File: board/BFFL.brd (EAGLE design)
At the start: 51 x 25.4 mm, 25 parts, among them IC1 LM317MSTT3, Q1 FDS5680, U1 ATTINY84-20SSU

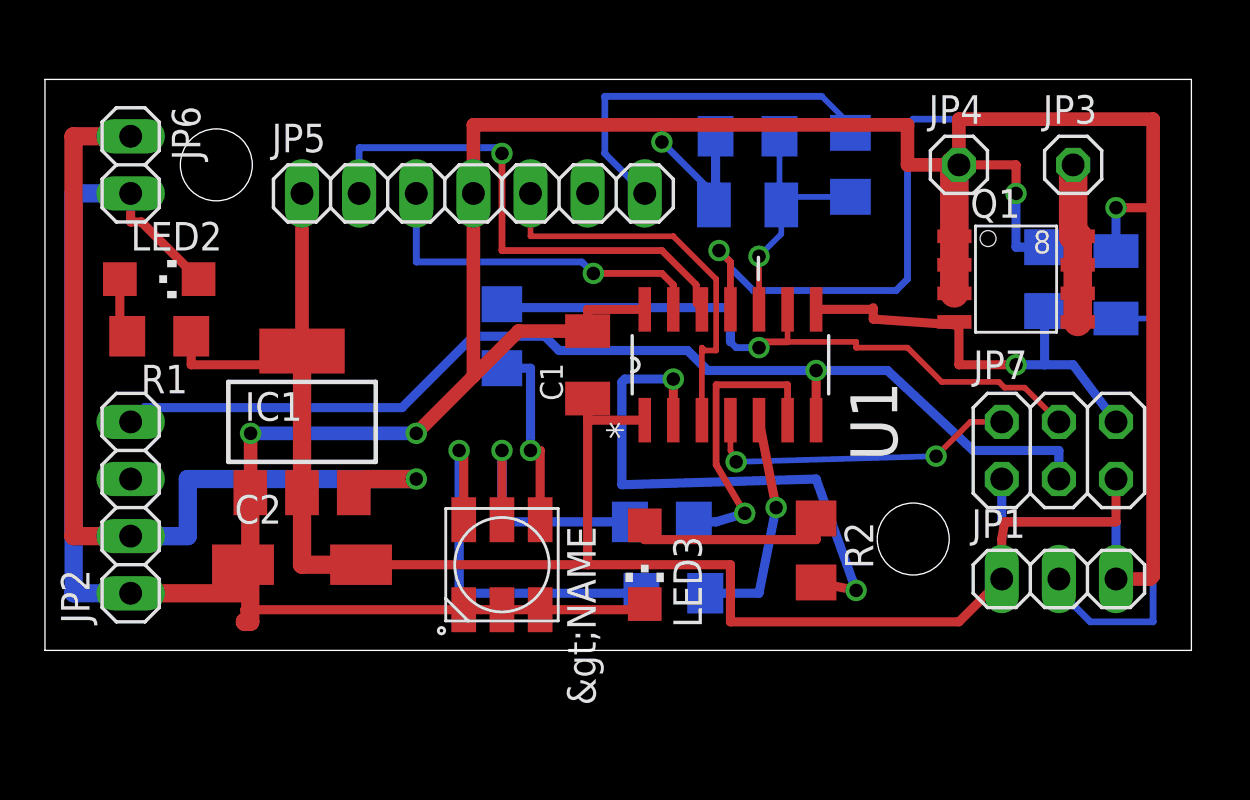
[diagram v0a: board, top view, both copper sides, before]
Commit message: Rev B of PCB, preliminary
Corrects multiple faults in Rev A and improves mounting options.
Silkscreen still needs to be done.
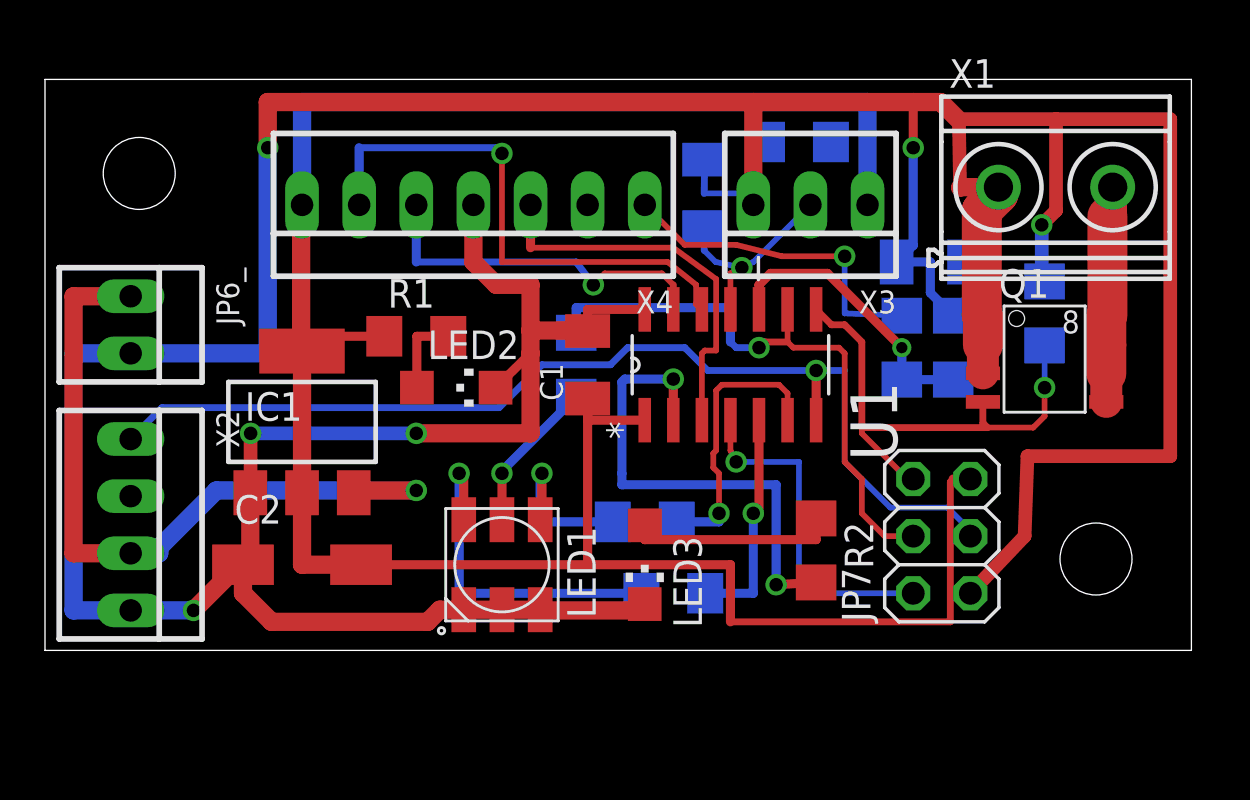
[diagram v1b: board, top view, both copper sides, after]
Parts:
- removed JP1: (no value), pinhead:1X03
- removed JP2: (no value), pinhead:1X04
- removed JP3, JP4: (no value), pinhead:1X01
- removed JP5: (no value), pinhead:1X07
- removed JP6: (no value), pinhead:1X02
- added JP6_: 22-23-2021, con-molex:22-23-2021
- added R8: (no value), rcl:R1206
- added X1: MKDSN1,5/2-5,08, con-phoenix-508:MKDSN1,5/2-5,08
- added X2: 22-23-2041, con-molex:22-23-2041
- added X3: 22-23-2031, con-molex:22-23-2031
- added X4: 22-23-2071, con-molex:22-23-2071
- JP7: value (none) -> AVRISP
- R6, R9: value (none) -> 10k
- R7: value (none) -> 1k
- moved C3 18.7 mm to (54.7, 20.3)
- moved LED2 14.1 mm to (43.7, 11.7)
- moved R7 13.1 mm to (65.8, 13.5), turned to 90 degrees
- moved R1 11.4 mm to (41.9, 14.0), turned to 0 degrees
- moved C4 8.52 mm to (64.8, 17.3)
- moved R9 8.44 mm to (63.5, 13.5)
- moved JP7 6.45 mm to (65.3, 5.08), turned to 90 degrees
- moved Q1 3.78 mm to (69.8, 13.0)
- moved R4 3.54 mm to (49.0, 12.7)
- moved R6 1.52 mm to (69.8, 15.0)
- moved R3 0.76 mm to (52.1, 5.71)
- renumbered LED4 to LED1
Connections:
- net N$1: now also X4.1; no longer JP5.7
- net N$10: now also R3.1; no longer R4.1
- net N$12: now also X1.2; no longer JP3.1
- net N$13: now also JP6_.2, R8.2, X1.1, X2.4, X3.3, X4.4; no longer JP1.3, JP2.1, JP4.1, JP5.4, JP6.2
- net N$16: now also X2.1; no longer JP2.4
- net N$17: now also X4.3; no longer JP5.5
- net N$19: now also R8.1, X3.2; no longer JP1.2
- net N$21: now also X4.5; no longer JP5.3
- net N$22: now also X4.6; no longer JP5.2
- net N$3: now also JP6_.1, X2.3; no longer JP2.2, JP6.1
- net N$6: now also X3.1, X4.7; no longer JP1.1, JP5.1
- net N$9: now also R4.1; no longer R3.1
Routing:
- net N$19: track 59.6 -> 9.46 mm
- net N$6: track 77.5 -> 107.3 mm
- net N$13: track 187.0 -> 212.6 mm, vias 5 -> 6
- net N$2: track 11.4 -> 20.6 mm
- net N$3: track 41.1 -> 33.3 mm
- net N$9: track 11.9 -> 6.84 mm
- net N$18: track 29.6 -> 26.6 mm
- net N$4: track 19.5 -> 22.5 mm
- net N$5: track 24.5 -> 21.8 mm
- net N$12: track 7.19 -> 9.67 mm
- net N$11: track 17.8 -> 15.7 mm
- net N$1: track 16.9 -> 14.8 mm, vias 0 -> 1
- net N$24: track 14.4 -> 15.6 mm, vias 2 -> 1
- net N$7: track 2.68 -> 3.68 mm
- net N$10: track 8.44 -> 7.46 mm
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
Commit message: Update board
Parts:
- renumbered IC1 to U2, JP6_ to JP1, JP7 to JP6, X1 to JP3, X2 to JP5, X3 to JP4, X4 to JP2
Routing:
- net N$13: track 212.6 -> 229.2 mm
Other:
- board text added: "BFFL"
- board text added: "REV B"
